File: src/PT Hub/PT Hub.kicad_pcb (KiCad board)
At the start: 2 copper layers, 100.3 x 46.5 mm, 18 parts, among them P1 20021511-00026T4LF, P2 CON_39299043, P3 CON_39299043, P4 CON_39299043, P5 CON_39299043, P6 CON_39299043, P7 CON_39299043, P8 CON_39299043, P9 CON_39299043

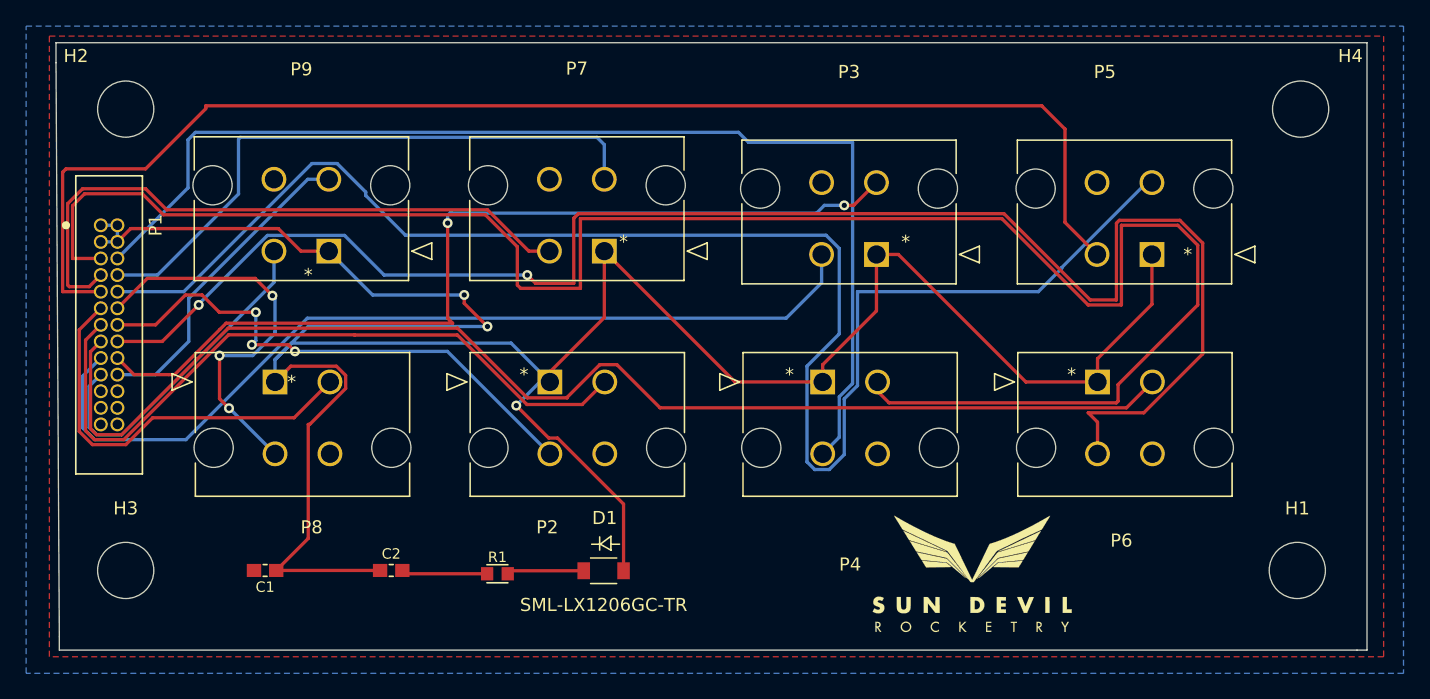
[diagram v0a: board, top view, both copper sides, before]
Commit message: rerouted PCB to handle ground plane discontinuities
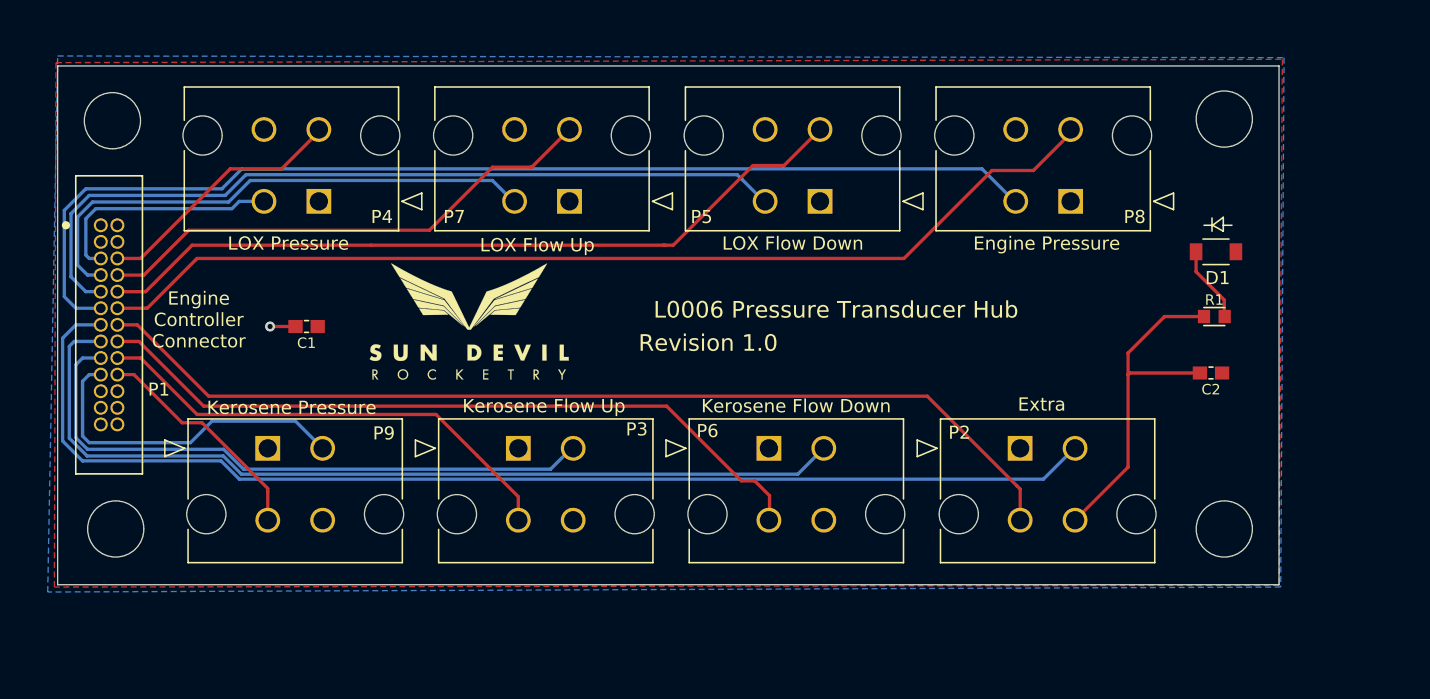
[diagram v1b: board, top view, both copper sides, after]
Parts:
- moved C2 64.5 mm to (159.3, 121.8), turned to 180 degrees
- moved P8 62.4 mm to (148.5, 108.7), turned to 0 degrees
- moved R1 58.3 mm to (159.5, 117.5)
- moved D1 52.8 mm to (159.6, 112.5)
- moved LOGO1 43.1 mm to (102.5, 117.6)
- moved P4 41.0 mm to (91.0, 108.7), turned to 0 degrees
- moved P2 36.3 mm to (144.7, 127.6)
- moved P3 31.2 mm to (106.2, 127.6), turned to 180 degrees
- moved P5 25.7 mm to (129.3, 108.7)
- moved P6 25.7 mm to (125.4, 127.6)
- moved C1 18.9 mm to (90.0, 118.2)
- moved P9 15.8 mm to (87.1, 127.6), turned to 180 degrees
- moved H1 6.43 mm to (160.3, 133.7)
- moved H4 5.89 mm to (160.3, 102.4)
- moved P7 4.65 mm to (110.2, 108.7)
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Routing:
- net 5V: track 205.4 -> 0.00 mm, vias 3 -> 0
- net PT1+: track 146.2 -> 18.2 mm
- net PT6-: track 125.1 -> 56.5 mm, vias 2 -> 0
- net PT1-: track 87.5 -> 19.5 mm
- net PT3-: track 122.0 -> 58.9 mm
- net PT4+: track 31.7 -> 84.5 mm
- net PT4-: track 30.6 -> 78.8 mm, vias 3 -> 0
- net PT3+: track 102.4 -> 62.6 mm
- net PT5+: track 54.9 -> 90.7 mm
- net PT5-: track 41.0 -> 76.7 mm, vias 3 -> 0
- net PT7-: track 70.1 -> 36.9 mm, vias 2 -> 0
- net PT6+: track 97.3 -> 69.2 mm
- net PT7+: track 70.0 -> 47.2 mm
- net Earth: track 6.59 -> 28.9 mm, vias 0 -> 1
- net PT2+: track 48.5 -> 40.5 mm
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- added copper zone on F.Cu, net 5V
- removed copper zone on F.Cu, net Earth
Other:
- board size 100.3 x 46.5 mm -> 93.5 x 39.7 mm
- board text added: "Engine Controller Connector"
- board text added: "Engine Pressure"
- board text added: "Extra"
- board text added: "Kerosene Flow Down"
- board text added: "Kerosene Flow Up"
- board text added: "Kerosene Pressure"
- board text added: "L0006 Pressure Transducer Hub"
- board text added: "LOX Flow Down"
- board text added: "LOX Flow Up"
- board text added: "LOX Pressure"
- board text added: "Revision 1.0"

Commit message: modified PT hub to be usable with hybrids PTs
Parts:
- LOGO1: value LOGO -> Logo
- P2, P3, P4, P5, P6, P7, P8, P9: value CON_39299043 -> 39299043
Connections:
- P1 pad 14: PT5- -> Earth
- P1 pad 16: PT6- -> Earth
- P1 pad 18: PT7- -> Earth
- P1 pad 20: PT8- -> Earth
- P1 pad 3: 5V -> VIN
- P1 pad 4: 5V -> VIN
- P2 pad 1: 5V -> VIN
- P2 pad 3: PT5- -> Earth
- P3 pad 1: 5V -> VIN
- P3 pad 3: PT7- -> Earth
- P6 pad 1: 5V -> VIN
- P6 pad 3: PT6- -> Earth
- P9 pad 1: 5V -> VIN
- P9 pad 3: PT8- -> Earth
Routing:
- net Earth: track 28.9 -> 216.5 mm
- net VIN: track 0.00 -> 110.9 mm, vias 0 -> 1
- net PT5-: track 76.7 -> 0.00 mm
- net PT6-: track 56.5 -> 0.00 mm
- net PT7-: track 36.9 -> 0.00 mm
- net PT8-: track 17.5 -> 0.00 mm
